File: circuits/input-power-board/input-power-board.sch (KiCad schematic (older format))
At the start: 9 parts, among them J1 HEADER-MALE-2POS-TH-1x02-P0.1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, J2 HEADER-MALE-2POS-TH-1x02-P0.1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, J3 HEADER-MALE-2POS-TH-1x02-P0.1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, J4 HEADER-MALE-2POS-TH-1x02-P0.1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, J5 BARREL_JACK, U1 NCP7805-5V, U2 LM1117

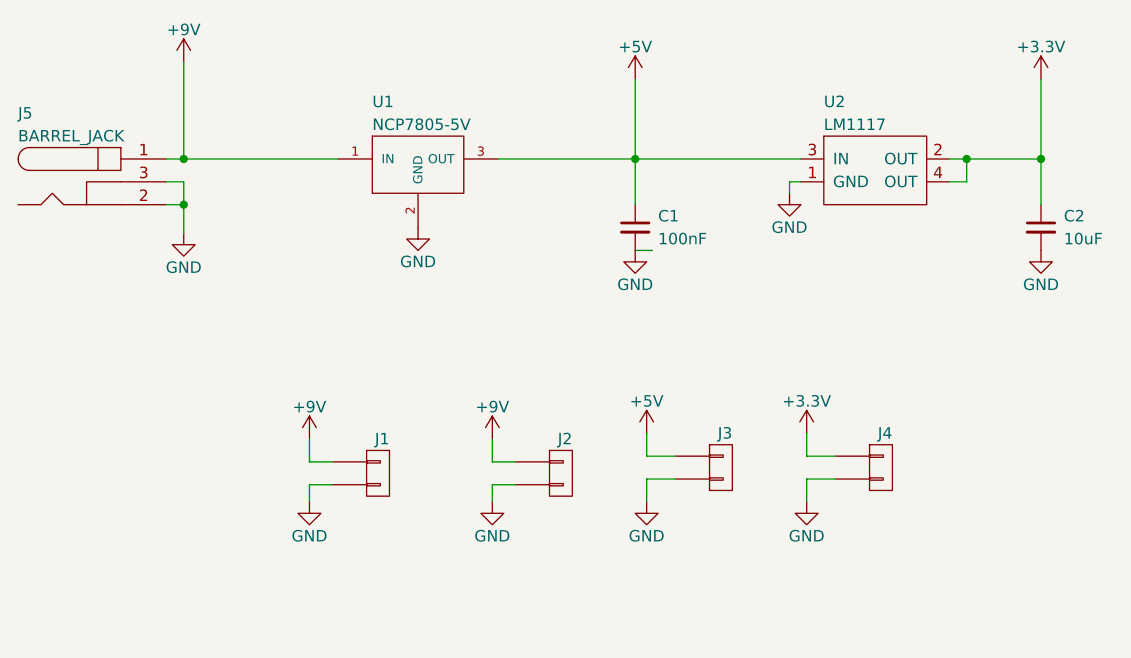
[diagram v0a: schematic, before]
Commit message: Updated input power board v1.1 and library.
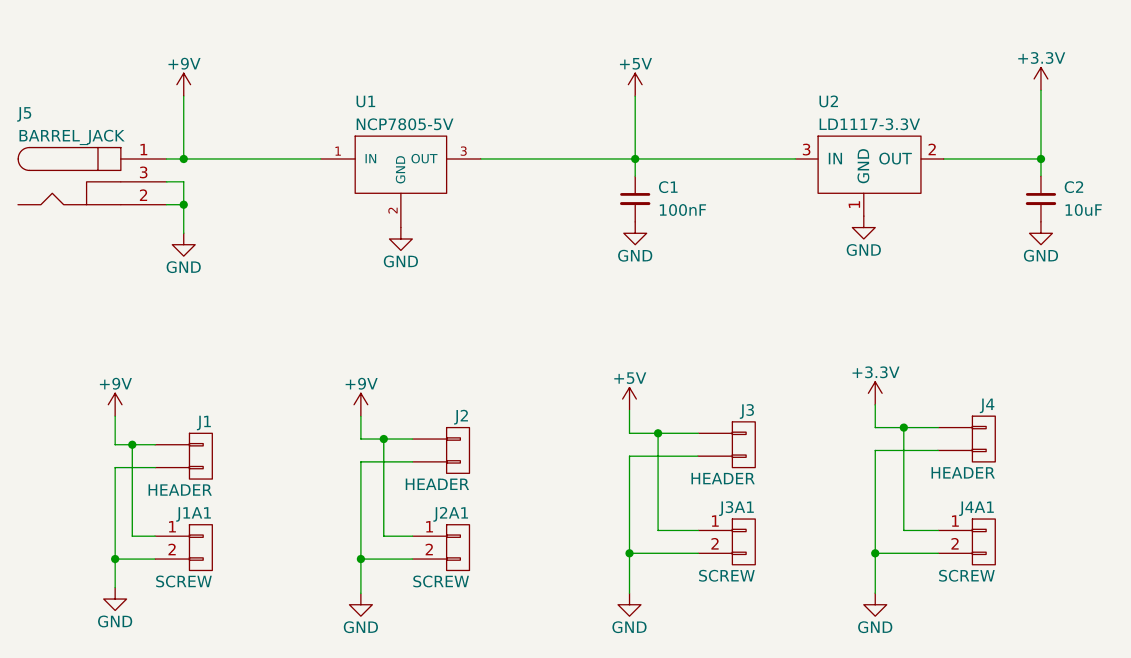
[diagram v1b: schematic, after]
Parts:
- removed C1: 100nF, Wickerlib:0805, symbol CAP-CER-0.1UF-25V-X7R-0805
- removed C2: 10uF, Wickerlib:1210, symbol CAP-CER-10UF-25V-X7R-1210
- removed U2: LM1117, Wickerlib:SOT-223, symbol IC-REG-LDO-3.3V-0.8A-LM1117-SOT223
- added C1: 100nF, Wickerlib:C_Disc_D7.5_P5, symbol CAP-CER-0.1UF-50V-C0G-RADIAL
- added C2: 10uF, Wickerlib:C_Disc_D3_P2.5, symbol CAP-CER-10UF-25V-X7R-RADIAL
- added J1A1, J2A1, J3A1, J4A1: SCREW, Wickerlib:OSTVN02A150, symbol CONN-TERM-SCREW-GREEN-2.54MM-2POS-TH
- added U2: LD1117-3.3V, Wickerlib:TO-220_Neutral123_Vertical_LargePads, symbol IC-REG-LDO-3.3V-1A-LD1117-TO220AB
- J1, J2, J3, J4: value HEADER-MALE-2POS-TH-1x02-P0.1IN -> HEADER
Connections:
- wire segments 30 -> 37
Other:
- moved on the sheet: J1, U1
